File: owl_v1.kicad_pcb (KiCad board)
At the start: 4 copper layers, 43.3 x 73.2 mm, 63 parts, among them J1 USB_C_Receptacle_USB2.0_16P, J10 JST-PH Battery, J3 Screw_Terminal_01x03, J4 SPI1_IMU, J5 I2C, J6 Micro_SD_Card_Det_Hirose_DM3AT, J7 I2C OLED, J8 External GPIOs, SW1 SW_SPDT, U1 STM32F103C8T6, U3 FT230XS, U4 SN65HVD230, U5 TLV73333PDBV, Y1 8MHz, Y2 32k768

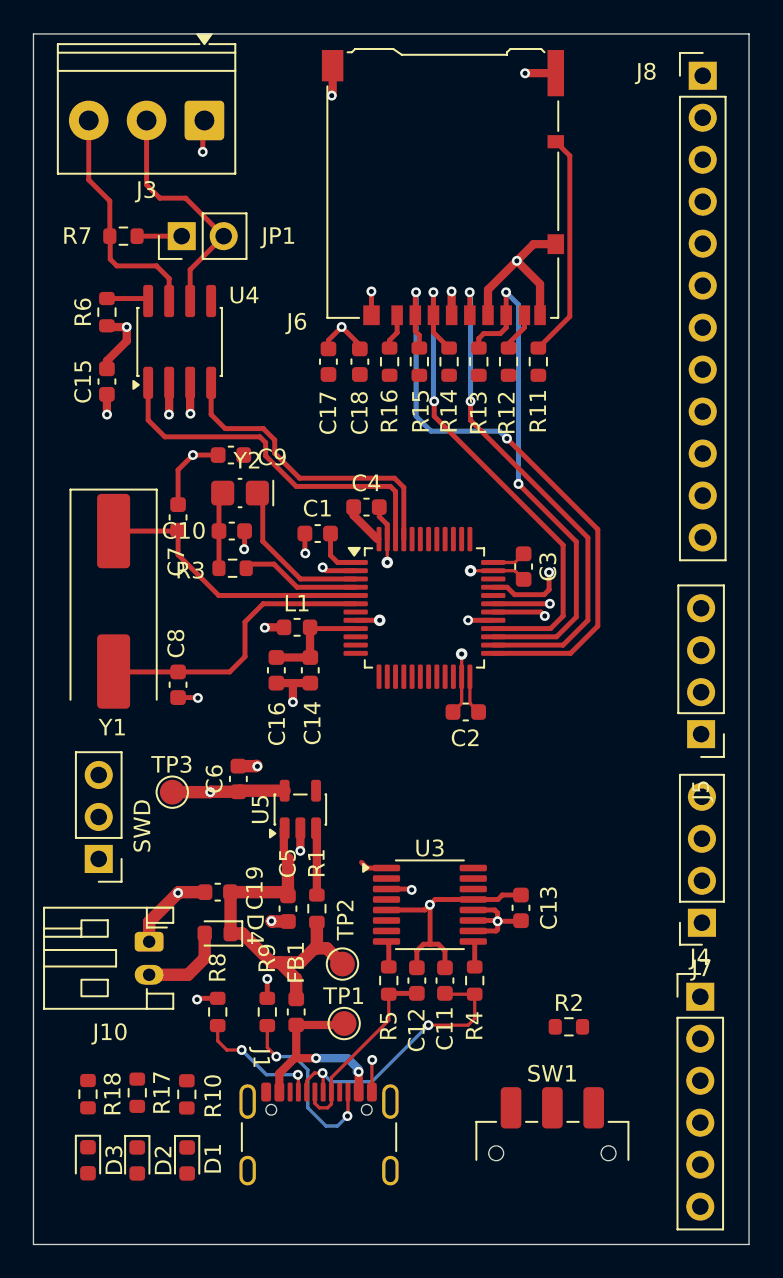
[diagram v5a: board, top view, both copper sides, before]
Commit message: [feat] Route most GPIO pins and SWD pins
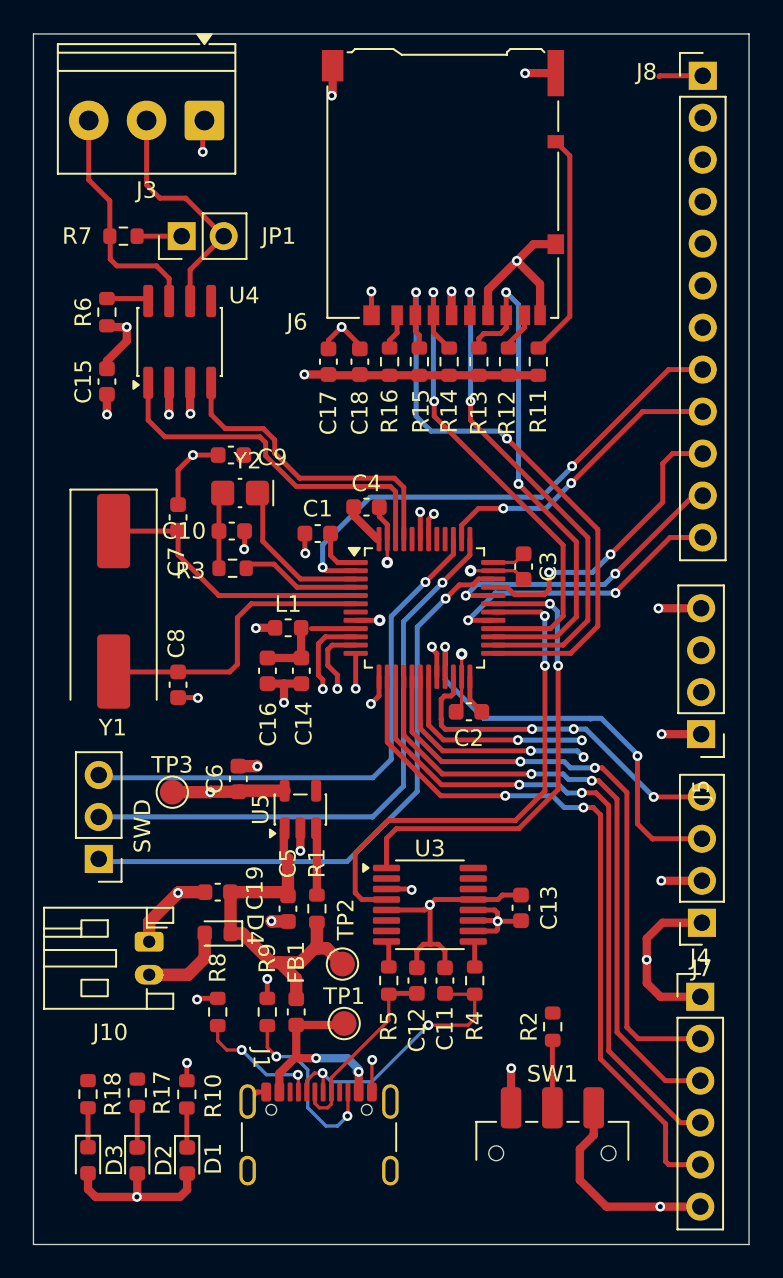
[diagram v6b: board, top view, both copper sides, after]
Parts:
- moved R2 0.98 mm to (182.5, 106.8), turned to 90 degrees
- moved C14 0.54 mm to (167.3, 85.3)
- moved C16 0.54 mm to (165.2, 85.3)
- moved L1 0.54 mm to (166.5, 82.7)
- moved C2 0.19 mm to (177.4, 87.8)
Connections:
- U1 pad 18: GPIO_9 -> GPIO_6
- U1 pad 19: GPIO_10 -> GPIO_5
- U1 pad 2: GPIO_8 -> GPIO_7
- U1 pad 20: GPIO_11 -> GPIO_4
- U1 pad 29: GPIO_4 -> GPIO_11
- U1 pad 32: GPIO_5 -> GPIO_10
- U1 pad 33: GPIO_6 -> GPIO_9
- U1 pad 38: GPIO_7 -> GPIO_8
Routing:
- net SPI1_CS: track 0.00 -> 43.5 mm, vias 0 -> 2
- net SPI1_SCK: track 0.00 -> 40.5 mm, vias 0 -> 2
- net +3.3V: track 31.0 -> 69.8 mm, vias 7 -> 12
- net SPI1_MISO: track 0.00 -> 38.4 mm, vias 0 -> 2
- net SWDIO: track 0.00 -> 36.8 mm, vias 0 -> 1
- net SPI1_MOSI: track 0.00 -> 36.8 mm, vias 0 -> 2
- net SWCLK: track 0.00 -> 35.8 mm, vias 0 -> 1
- net TRACE_SWO: track 0.00 -> 33.1 mm, vias 0 -> 1
- net GPIO_7: track 0.00 -> 30.8 mm, vias 0 -> 2
- net /owl_v1/USB to UART Bridge/FT230_RXD: track 3.22 -> 31.3 mm, vias 1 -> 2
- net OLED_SCLK: track 0.00 -> 25.9 mm, vias 0 -> 2
- net /owl_v1/USB to UART Bridge/FT230_TXD: track 5.08 -> 28.3 mm, vias 1 -> 2
- net OLED_SDA: track 0.00 -> 21.1 mm, vias 0 -> 3
- net GND: track 79.6 -> 99.6 mm, vias 26 -> 30
- net GPIO_10: track 0.00 -> 18.5 mm, vias 0 -> 2
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
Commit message: [feat] Connect 3.3V source to all pins requiring 3.3V
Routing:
- net +3.3V: track 69.8 -> 79.1 mm, vias 12 -> 15
- net +3.3VA: track 7.03 -> 7.66 mm
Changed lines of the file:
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@@
+	)
+	(segment
+		(start 170.425 75.4)
+		(end 169.03 75.4)
+		(width 0.5)
+		(layer "F.Cu")
+		(net "+3.3V")
+	)
+	(segment
+		(start 169.03 75.4)
+		(end 167.12 75.4)
+		(width 0.5)
+		(layer "F.Cu")
+		(net "+3.3V")
 	)
 	(segment
@@
 	)
 	(segment
+		(start 180.66 76.86)
+		(end 180.66 78.175)
+		(width 0.5)
+		(layer "F.Cu")
+		(net "+3.3V")
+	)
+	(segment
+		(start 167.12 75.4)
+		(end 167.11 75.41)
+		(width 0.5)
+		(layer "F.Cu")
+		(net "+3.3V")
+	)
+	(segment
 		(start 189.06 89.14)
 		(end 191.45 89.14)
@@
 	)
 	(segment
+		(start 180.14 86.58)
+		(end 180.14 87.42)
+		(width 0.5)
+		(layer "F.Cu")
+		(net "+3.3V")
+	)
+	(segment
 		(start 188.16 102.79)
 		(end 188.16 101.5)
@@
 		(end 180.55 100.425)
 		(width 0.3)
+		(layer "F.Cu")
+		(net "+3.3V")
+	)
+	(segment
+		(start 180.66 78.175)
+		(end 180.71 78.225)
+		(width 0.5)
 		(layer "F.Cu")
 		(net "+3.3V")
@@
 	)
 	(segment
+		(start 180.14 87.42)
+		(end 179.77 87.79)
+		(width 0.5)
+		(layer "F.Cu")
+		(net "+3.3V")
+	)
+	(segment
 		(start 179.05 101.05)
 		(end 179.1375 100.9625)
@@
 	)
 	(segment
+		(start 179.77 87.79)
+		(end 178.175 87.79)
+		(width 0.5)
+		(layer "F.Cu")
+		(net "+3.3V")
+	)
+	(segment
 		(start 161.775 92.625)
 		(end 161.75 92.65)
@@
 		(end 169.45 78.75)
 		(width 0.3)
+		(layer "F.Cu")
+		(net "+3.3V")
+	)
+	(segment
+		(start 169.025 75.755)
+		(end 169.025 77)
+		(width 0.5)
+		(layer "F.Cu")
+		(net "+3.3V")
+	)
+	(segment
+		(start 169.03 75.4)
+		(end 169.03 75.75)
+		(width 0.5)
 		(layer "F.Cu")
 		(net "+3.3V")
@@
 	)
 	(segment
+		(start 169.03 75.75)
+		(end 169.025 75.755)
+		(width 0.5)
+		(layer "F.Cu")
+		(net "+3.3V")
+	)
+	(segment
 		(start 178.955 99.78)
 		(end 179.1375 99.9625)
@@
 	)
 	(via
+		(at 167.11 75.41)
+		(size 0.6)
+		(drill 0.3)
+		(layers "F.Cu" "B.Cu")
+		(net "+3.3V")
+	)
+	(via
 		(at 164.51 82.73)
 		(size 0.6)
@@
 		(drill 0.3)
 		(layers "F.Cu" "B.Cu")
+		(net "+3.3V")
+	)
+	(via
+		(at 180.66 76.86)
+		(size 0.6)
+		(drill 0.3)
+		(layers "F.Cu" "B.Cu")
+		(free yes)
+		(net "+3.3V")
+	)
+	(via
+		(at 180.14 86.58)
+		(size 0.6)
+		(drill 0.3)
+		(layers "F.Cu" "B.Cu")
+		(free yes)
 		(net "+3.3V")
 	)
@@
 	)
 	(segment
-		(start 170.5475 82.75)
-		(end 167.8625 82.75)
+		(start 167.2925 82.75)
+		(end 167.2475 82.705)
 		(width 0.3)
 		(layer "F.Cu")
@@
 		(width 0.3)
 		(layer "F.Cu")
+		(net "+3.3VA")
+	)
+	(segment
+		(start 170.5475 82.75)
+		(end 167.2925 82.75)
+		(width 0.3)
+		(layer "F.Cu")

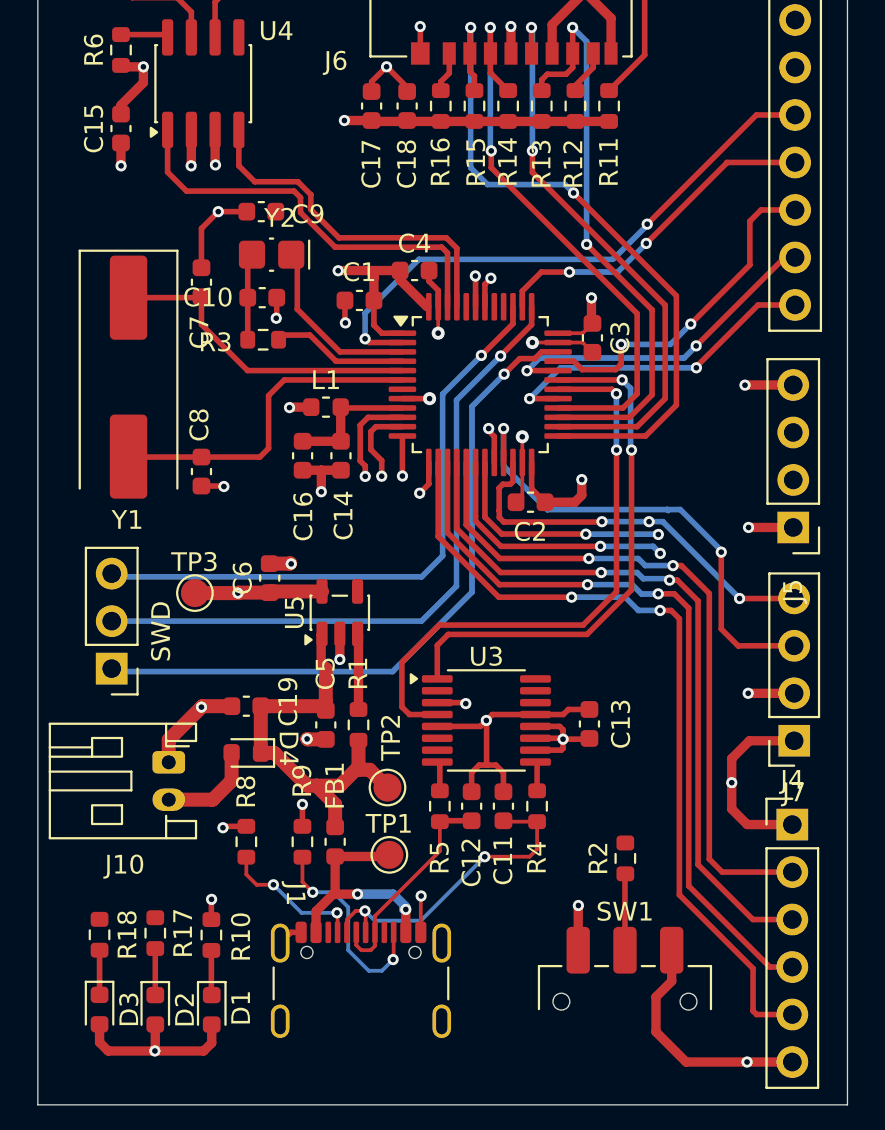
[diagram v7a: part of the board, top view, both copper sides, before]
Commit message: [refactor] Change how GPIO is routed
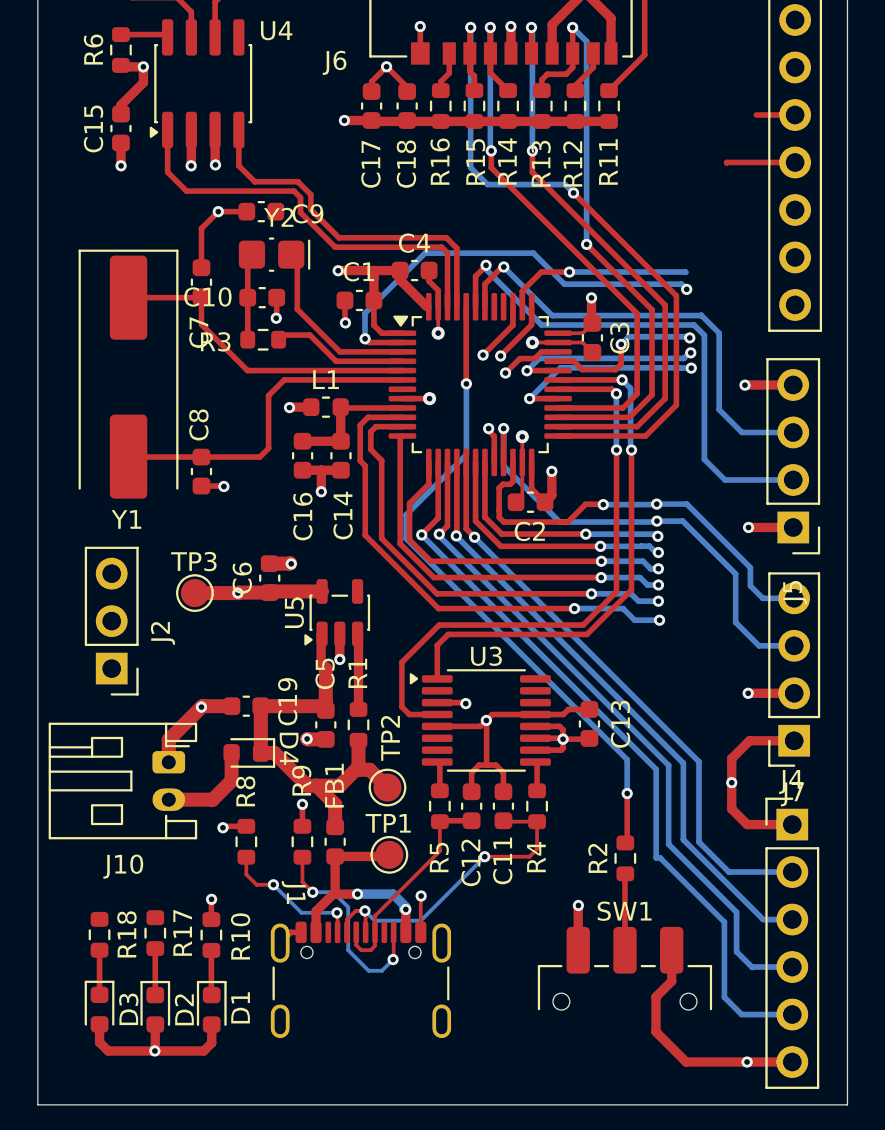
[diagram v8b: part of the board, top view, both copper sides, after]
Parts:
- renumbered SWD to J2
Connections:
- U1 pad 10: GPIO_0 -> GPIO_8
- U1 pad 38: GPIO_8 -> GPIO_0
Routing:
- net Net-(U1-BOOT0): track 0.00 -> 35.1 mm, vias 0 -> 2
- net SWDIO: track 36.8 -> 3.28 mm
- net SWCLK: track 35.8 -> 3.31 mm
- net TRACE_SWO: track 33.1 -> 3.25 mm
- net I2C_SDA: track 1.65 -> 27.6 mm
- net I2C_SCLK: track 1.66 -> 24.2 mm
- net GPIO_1: track 4.42 -> 23.9 mm, vias 1 -> 2
- net GPIO_2: track 2.14 -> 20.5 mm, vias 1 -> 2
- net GPIO_3: track 1.85 -> 18.5 mm, vias 1 -> 2
- net GPIO_8: track 18.3 -> 29.7 mm
- net GPIO_9: track 18.4 -> 8.60 mm
- net GPIO_10: track 18.5 -> 10.8 mm
- net GPIO_11: track 17.8 -> 10.9 mm
- net GPIO_7: track 30.8 -> 24.9 mm
- net SPI1_MOSI: track 36.8 -> 31.1 mm, vias 2 -> 1
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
